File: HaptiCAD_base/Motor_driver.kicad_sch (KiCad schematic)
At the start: 29 parts, among them J101 BLDC, U601 TMC6300-LA-T, U602 LMV321

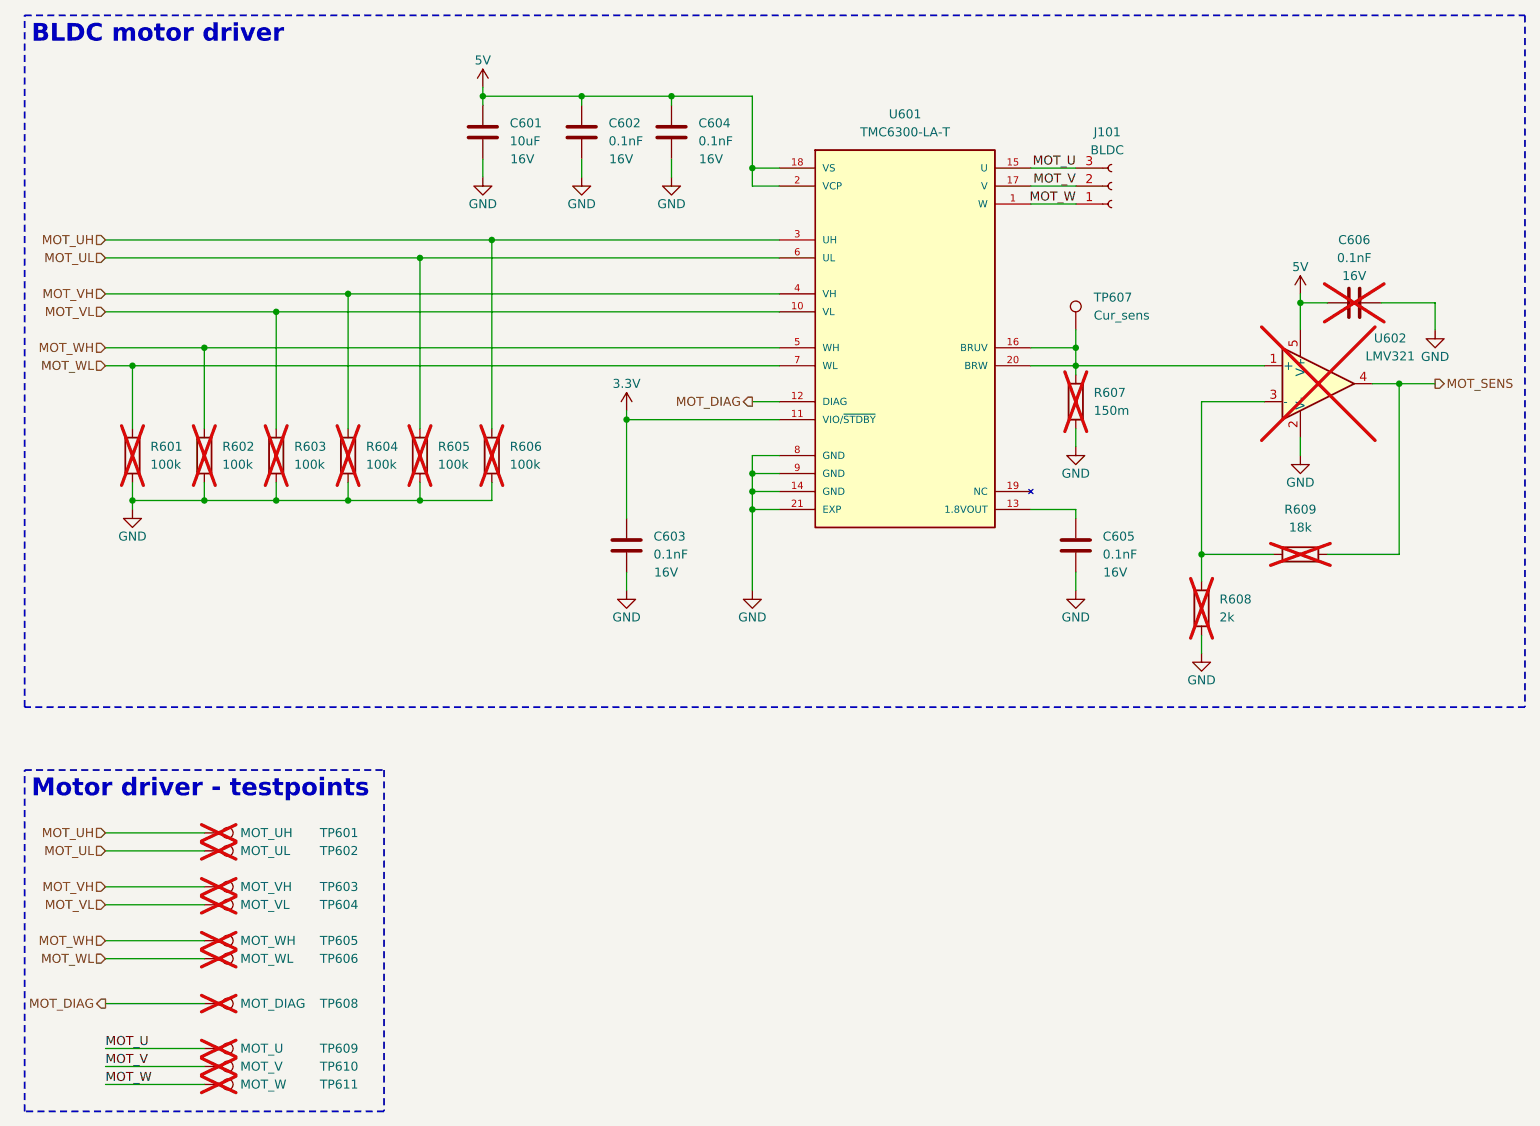
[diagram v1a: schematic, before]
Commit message: updated base schematic and PCB
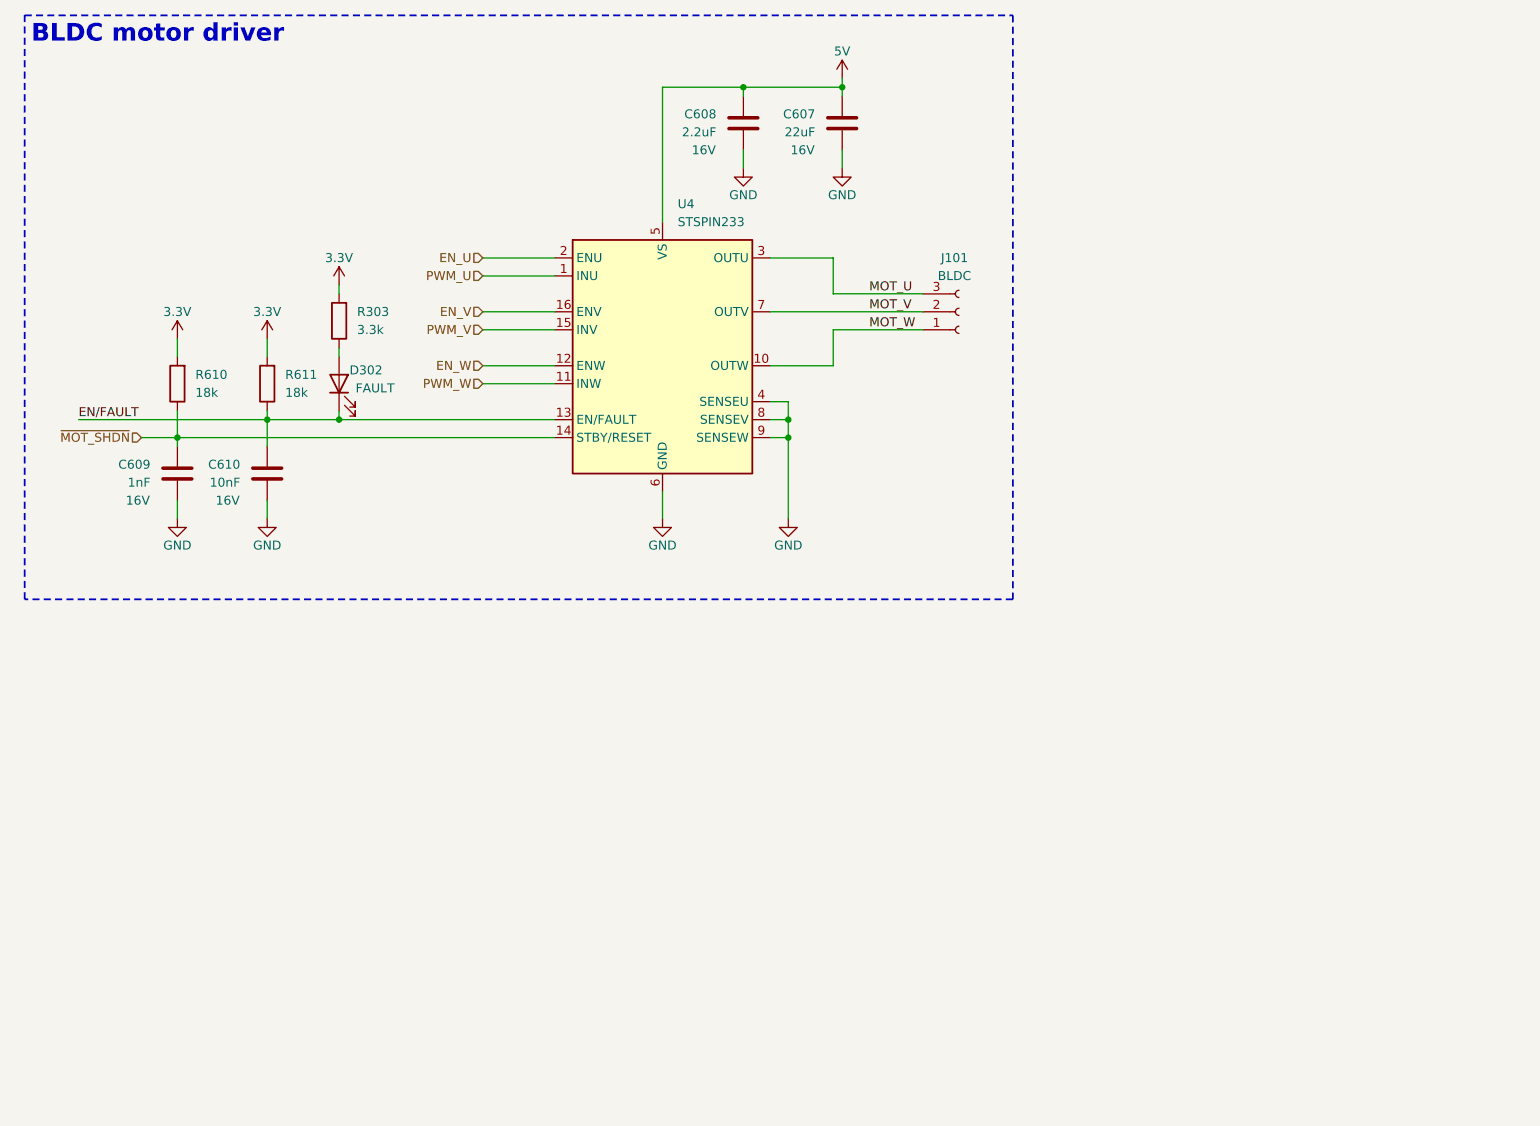
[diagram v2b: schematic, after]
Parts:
- removed C601: 10uF, Capacitor_SMD:C_0805_2012Metric, symbol Device:C
- removed C602, C603, C604, C605, C606: 0.1nF, Capacitor_SMD:C_0603_1608Metric, symbol Device:C
- removed R601, R602, R603, R604, R605, R606: 100k, Resistor_SMD:R_0402_1005Metric, symbol Device:R
- removed R607: 150m, Resistor_SMD:R_1206_3216Metric, symbol Device:R
- removed R608: 2k, Resistor_SMD:R_0603_1608Metric, symbol Device:R
- removed R609: 18k, Resistor_SMD:R_0603_1608Metric, symbol Device:R
- removed TP601: MOT_UH, TestPoint:TestPoint_Pad_D1.0mm, symbol Connector:TestPoint
- removed TP602: MOT_UL, TestPoint:TestPoint_Pad_D1.0mm, symbol Connector:TestPoint
- removed TP603: MOT_VH, TestPoint:TestPoint_Pad_D1.0mm, symbol Connector:TestPoint
- removed TP604: MOT_VL, TestPoint:TestPoint_Pad_D1.0mm, symbol Connector:TestPoint
- removed TP605: MOT_WH, TestPoint:TestPoint_Pad_D1.0mm, symbol Connector:TestPoint
- removed TP606: MOT_WL, TestPoint:TestPoint_Pad_D1.0mm, symbol Connector:TestPoint
- removed TP607: Cur_sens, TestPoint:TestPoint_Pad_D1.0mm, symbol Connector:TestPoint
- removed TP608: MOT_DIAG, TestPoint:TestPoint_Pad_D1.0mm, symbol Connector:TestPoint
- removed TP609: MOT_U, TestPoint:TestPoint_Pad_D1.0mm, symbol Connector:TestPoint
- removed TP610: MOT_V, TestPoint:TestPoint_Pad_D1.0mm, symbol Connector:TestPoint
- removed TP611: MOT_W, TestPoint:TestPoint_Pad_D1.0mm, symbol Connector:TestPoint
- removed U601: TMC6300-LA-T, TMC6300:QFN40P300X300X90-21N, symbol TMC6300:TMC6300-LA-T
- removed U602: LMV321, Package_TO_SOT_SMD:SOT-23-5, symbol Amplifier_Operational:LMV321
- added C607: 22uF, Capacitor_SMD:C_0805_2012Metric, symbol Device:C
- added C608: 2.2uF, Capacitor_SMD:C_0603_1608Metric, symbol Device:C
- added C609: 1nF, Capacitor_SMD:C_0603_1608Metric, symbol Device:C
- added C610: 10nF, Capacitor_SMD:C_0603_1608Metric, symbol Device:C
- added D302: FAULT, Diode_SMD:D_0603_1608Metric, symbol Device:LED
- added R303: 3.3k, Resistor_SMD:R_0402_1005Metric, symbol Device:R
- added R610, R611: 18k, Resistor_SMD:R_0402_1005Metric, symbol Device:R
- added U4: STSPIN233, Package_DFN_QFN:VQFN-16-1EP_3x3mm_P0.5mm_EP1.8x1.8mm, symbol Driver_Motor:STSPIN233
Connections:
- net 3.3V: now also R303.2, R610.2, R611.2
- net 5V: now also C607.1, C608.1, U4.5 (VS)
- net GND: now also C607.2, C608.2, C609.2, C610.2, U4.17 (GND), U4.4 (SENSEU), U4.6 (GND), U4.8 (SENSEV), U4.9 (SENSEW)
- net MOT_U: now also U4.3 (OUTU)
- net MOT_V: now also U4.7 (OUTV)
- net MOT_W: now also U4.10 (OUTW)
- new net: D302.2 (A), R303.1
- new net EN_U: U4.2 (ENU)
- new net EN_V: U4.16 (ENV)
- new net EN_W: U4.12 (ENW)
- new net EN/FAULT: C610.1, D302.1 (K), R611.1, U4.13 (EN/FAULT)
- new net PWM_U: U4.1 (INU)
- new net PWM_V: U4.15 (INV)
- new net PWM_W: U4.11 (INW)
- new net ~{MOT_SHDN}: C609.1, R610.1, U4.14 (STBY/RESET)

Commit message: Finished schematic of the base board
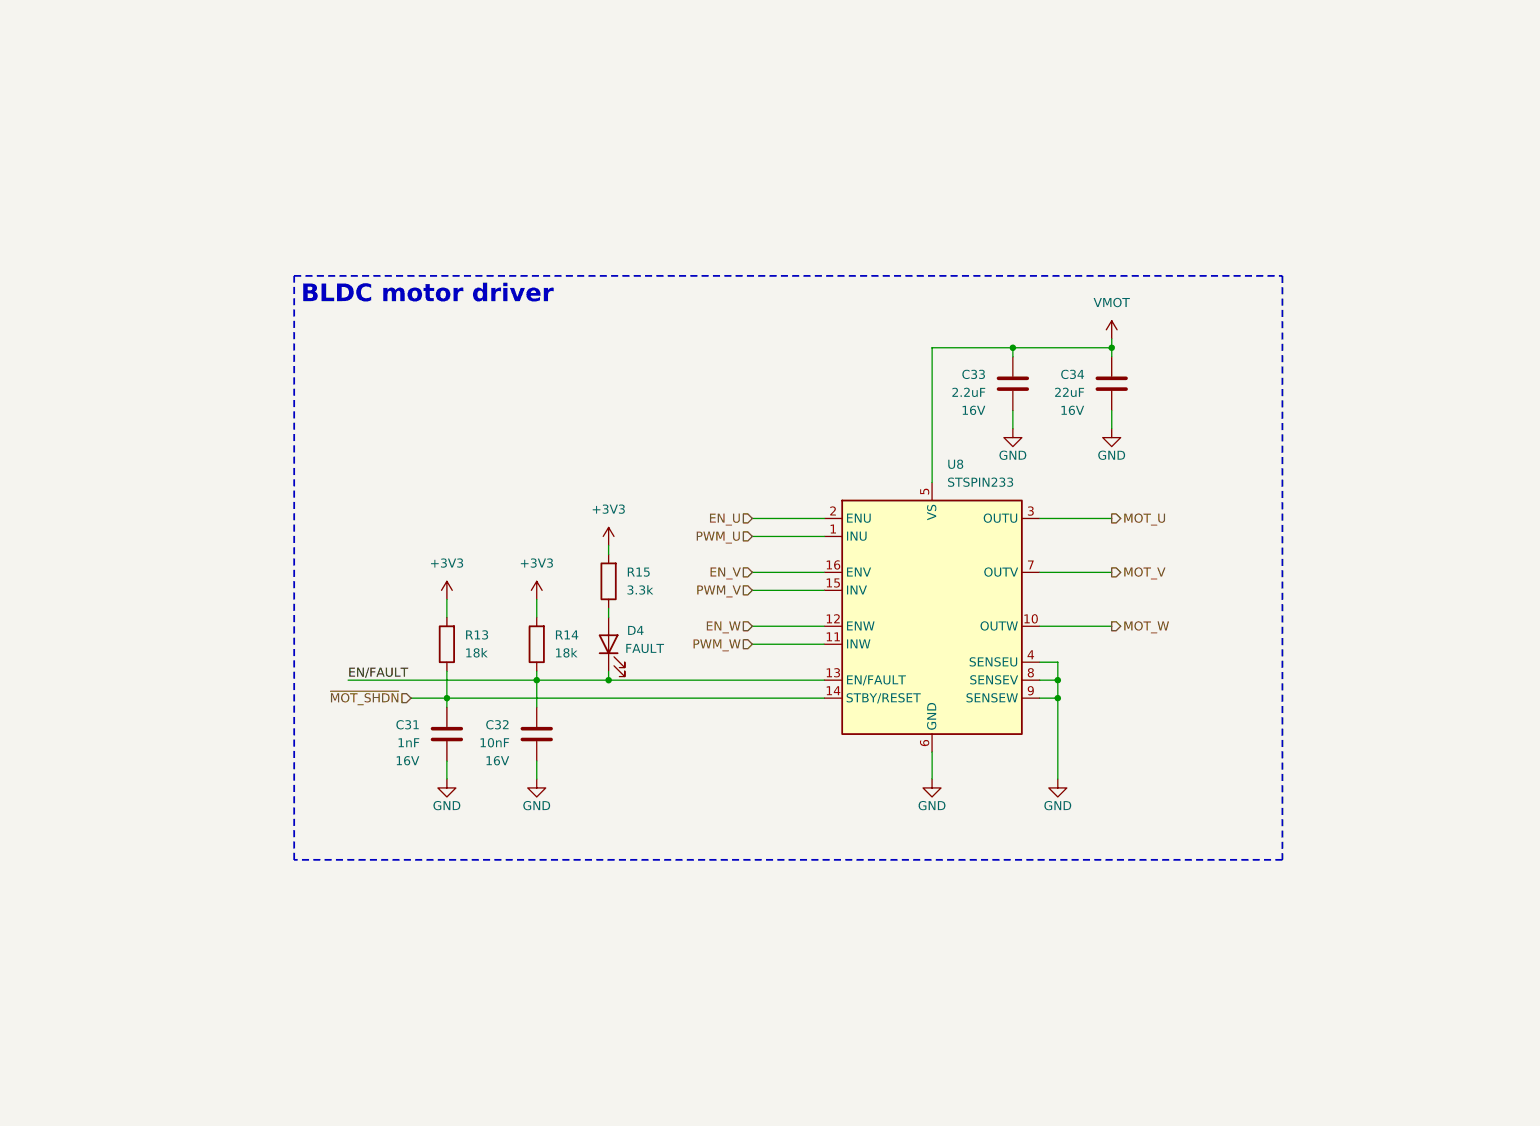
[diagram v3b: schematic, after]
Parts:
- removed J101: BLDC, Connector_Molex:Molex_SPOX_5267-03A_1x03_P2.50mm_Vertical, symbol Connector:Conn_01x03_Socket
- renumbered C609 to C31, C610 to C32, C608 to C33, C607 to C34, D302 to D4, R610 to R13, R611 to R14, R303 to R15, U4 to U8
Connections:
- net 3.3V renamed +3V3
- net 5V renamed VMOT
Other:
- moved on the sheet: C31, C32, C33, C34, D4, R13, R14, R15, U8

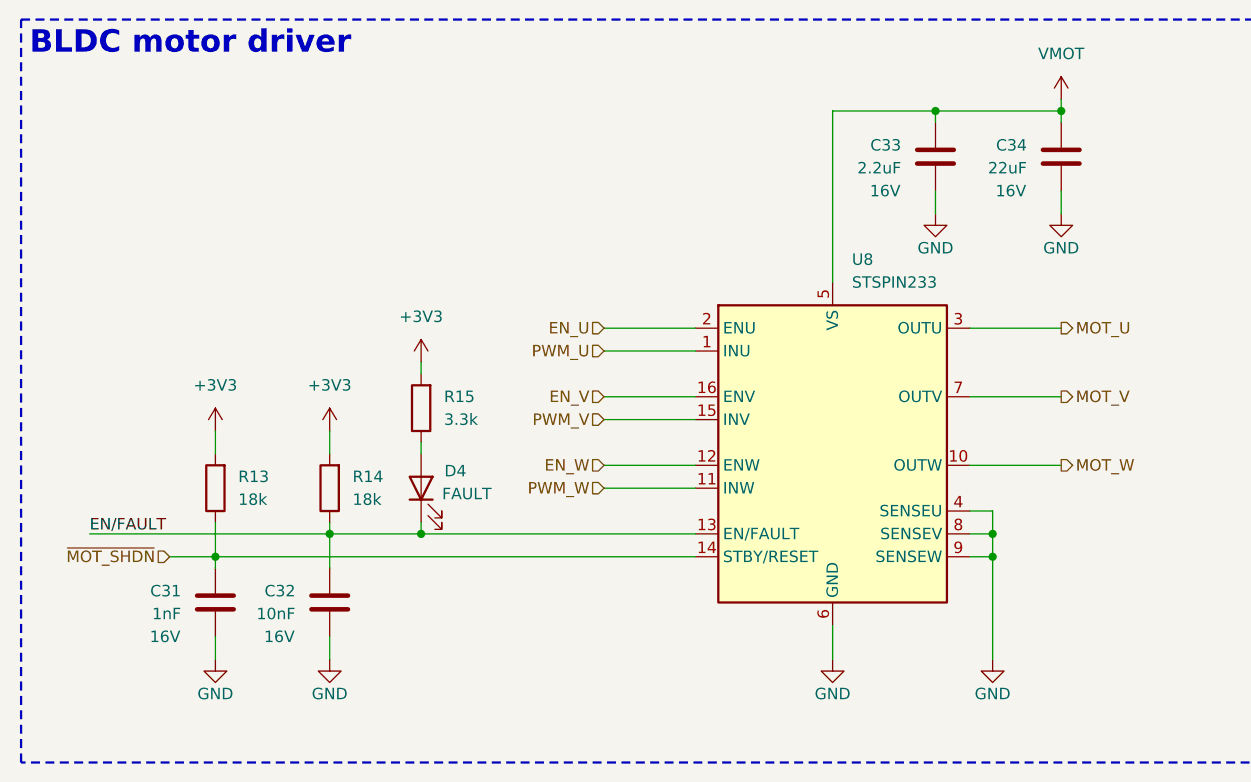
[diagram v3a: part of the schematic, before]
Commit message: Finished the layout for the base and motor mount
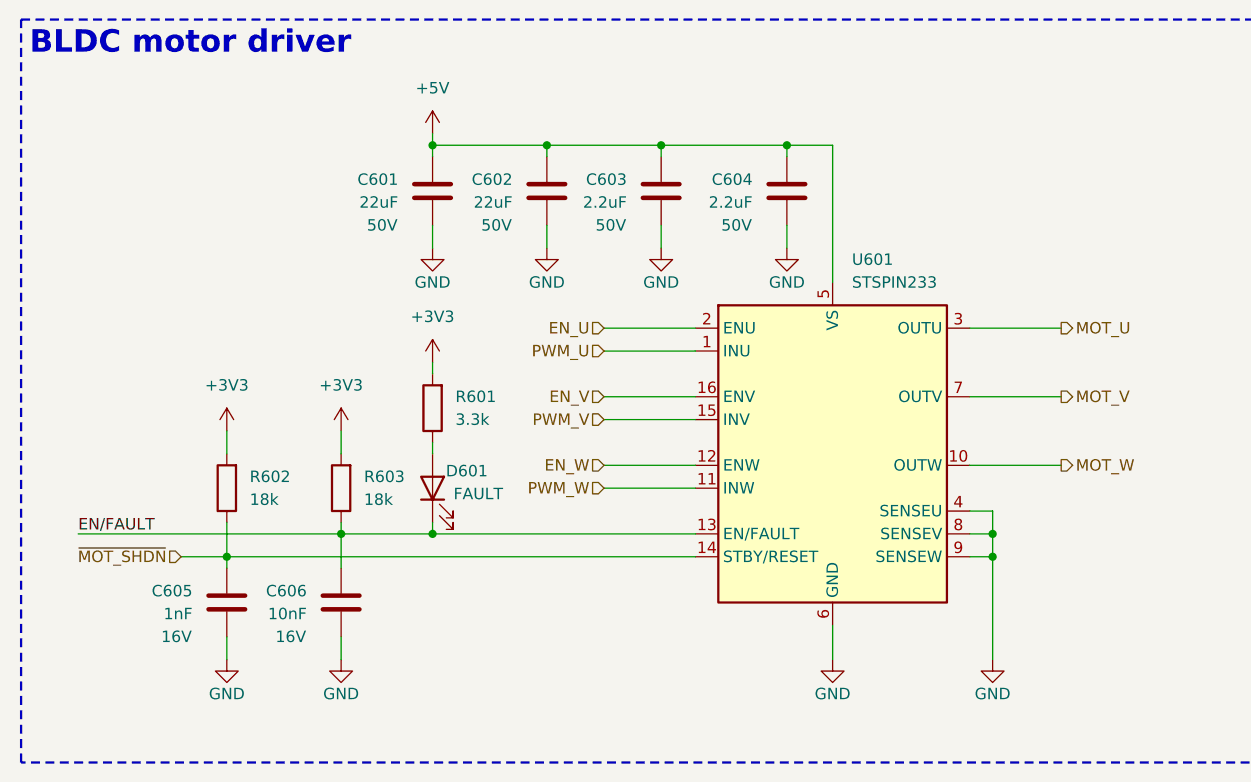
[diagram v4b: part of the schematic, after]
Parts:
- added C601: 22uF, Capacitor_SMD:C_0805_2012Metric, symbol Device:C
- added C603: 2.2uF, Capacitor_SMD:C_0805_2012Metric, symbol Device:C
- C602: renamed from C34; Voltage 16V -> 50V
- C604: renamed from C33; footprint Capacitor_SMD:C_0603_1608Metric -> Capacitor_SMD:C_0805_2012Metric; Voltage 16V -> 50V
- C605: renamed from C31; footprint Capacitor_SMD:C_0603_1608Metric -> Capacitor_SMD:C_0402_1005Metric
- C606: renamed from C32; footprint Capacitor_SMD:C_0603_1608Metric -> Capacitor_SMD:C_0402_1005Metric
- renumbered D4 to D601, R15 to R601, R13 to R602, R14 to R603, U8 to U601
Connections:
- net GND: now also C601.2, C603.2
- net VMOT renamed +5V
- net +5V: now also C601.1, C603.1
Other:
- moved on the sheet: C602, C604, C605, C606, D601, R601, R602, R603
